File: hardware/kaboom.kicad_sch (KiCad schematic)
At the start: 40 parts, among them SW1 SW_DP3T

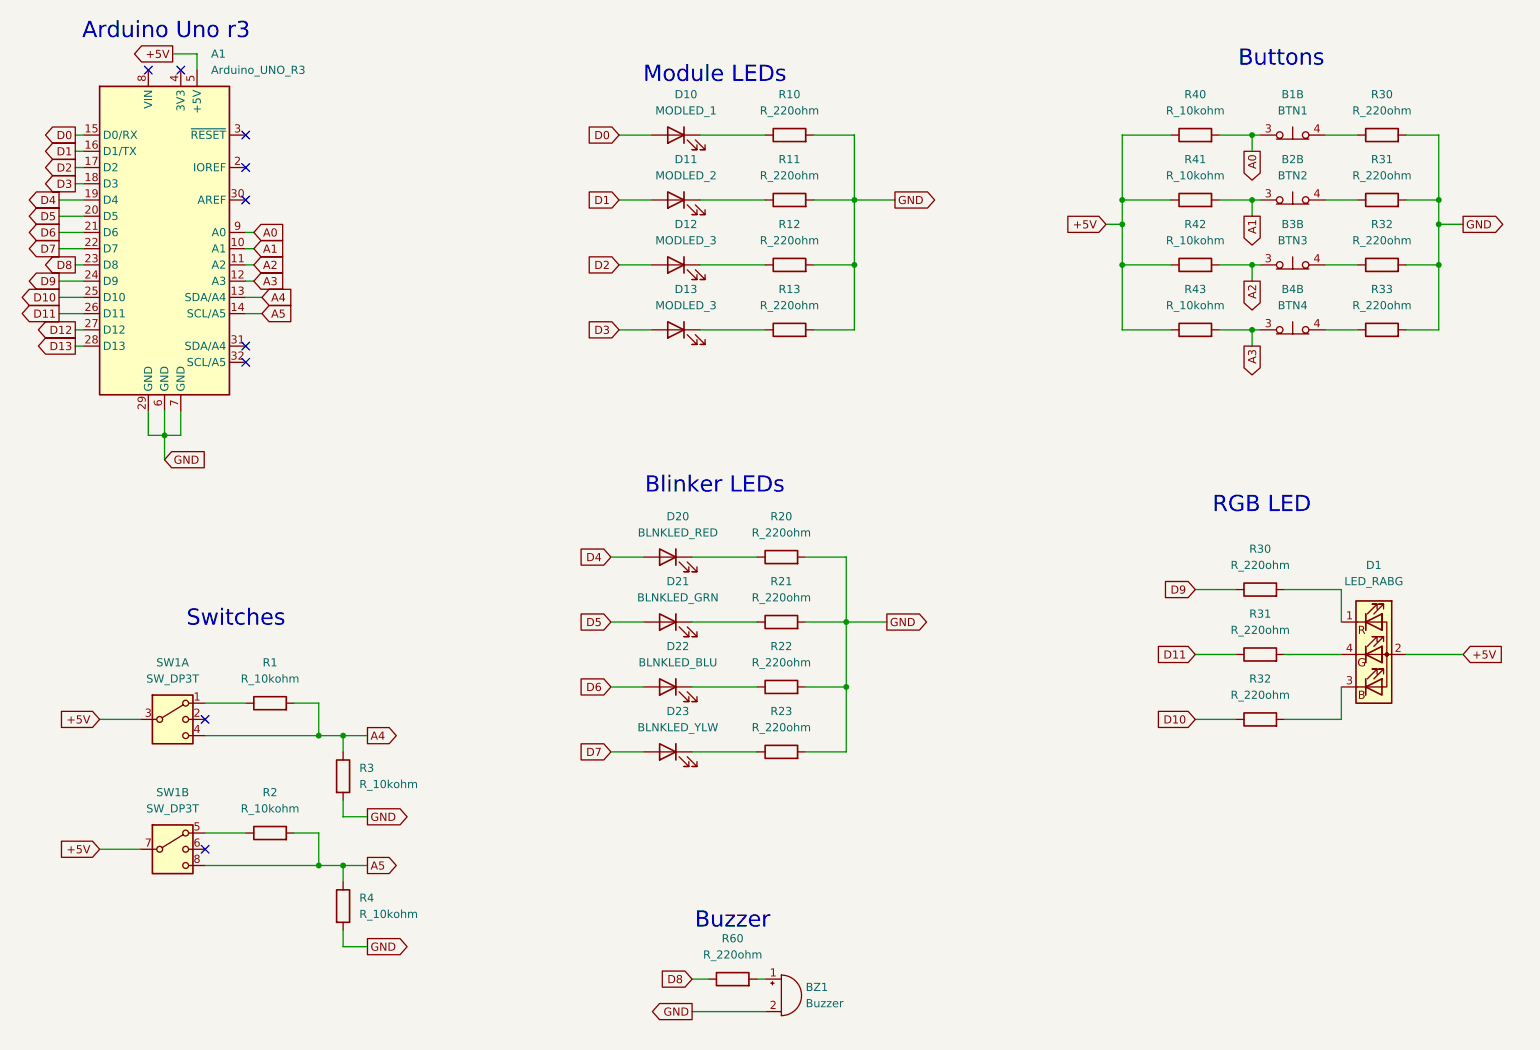
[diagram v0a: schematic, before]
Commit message: Updated coupling diagram
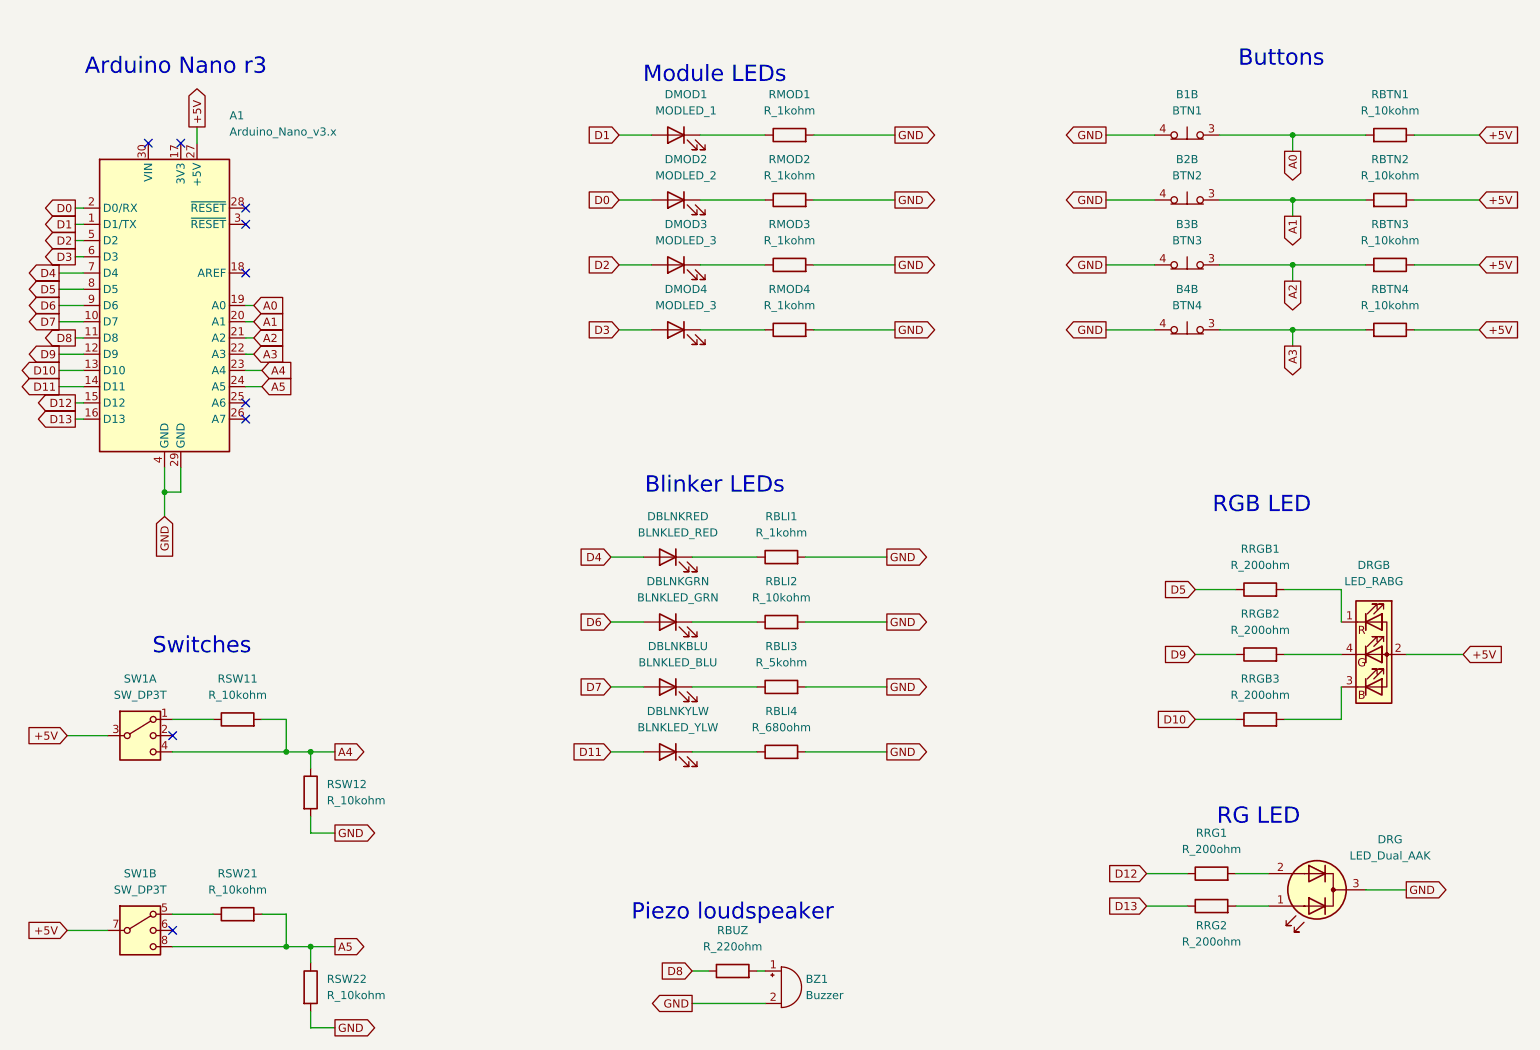
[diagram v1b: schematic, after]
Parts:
- removed A1: Arduino_UNO_R3, Module:Arduino_UNO_R3, symbol MCU_Module:Arduino_UNO_R3
- removed R30, R31, R32, R33: R_220ohm, symbol Device:R
- added A1: Arduino_Nano_v3.x, Module:Arduino_Nano, symbol MCU_Module:Arduino_Nano_v3.x
- added DRG: LED_Dual_AAK, symbol Device:LED_Dual_AAK
- added RRG1, RRG2: R_200ohm, symbol Device:R
- RBLI1: renamed from R20; value R_220ohm -> R_1kohm
- RBLI2: renamed from R21; value R_220ohm -> R_10kohm
- RBLI3: renamed from R22; value R_220ohm -> R_5kohm
- RBLI4: renamed from R23; value R_220ohm -> R_680ohm
- RMOD1: renamed from R10; value R_220ohm -> R_1kohm
- RMOD2: renamed from R11; value R_220ohm -> R_1kohm
- RMOD3: renamed from R12; value R_220ohm -> R_1kohm
- RMOD4: renamed from R13; value R_220ohm -> R_1kohm
- RRGB1: renamed from R30; value R_220ohm -> R_200ohm
- RRGB2: renamed from R31; value R_220ohm -> R_200ohm
- RRGB3: renamed from R32; value R_220ohm -> R_200ohm
- renumbered D22 to DBLNKBLU, D21 to DBLNKGRN, D20 to DBLNKRED, D23 to DBLNKYLW, D10 to DMOD1, D11 to DMOD2, D12 to DMOD3, D13 to DMOD4, D1 to DRGB, R40 to RBTN1, R41 to RBTN2, R42 to RBTN3, R43 to RBTN4, R60 to RBUZ, R1 to RSW11, R3 to RSW12, R2 to RSW21, R4 to RSW22
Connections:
- net +5V: now also A1.27 (+5V)
- net A0: now also A1.19 (A0)
- net A1: now also A1.20 (A1)
- net A2: now also A1.21 (A2)
- net A3: now also A1.22 (A3)
- net A4: now also A1.23 (A4)
- net A5: now also A1.24 (A5)
- net D0: now also DMOD2.2 (A), A1.2 (D0/RX); no longer DMOD1.2 (A)
- net D1: now also DMOD1.2 (A), A1.1 (D1/TX); no longer DMOD2.2 (A)
- net D10: now also A1.13 (D10)
- net D11: now also DBLNKYLW.2 (A), A1.14 (D11); no longer RRGB2.1
- net D12: now also A1.15 (D12), RRG1.1
- net D13: now also A1.16 (D13), RRG2.1
- net D2: now also A1.5 (D2)
- net D3: now also A1.6 (D3)
- net D4: now also A1.7 (D4)
- net D5: now also RRGB1.1, A1.8 (D5); no longer DBLNKGRN.2 (A)
- net D6: now also DBLNKGRN.2 (A), A1.9 (D6); no longer DBLNKBLU.2 (A)
- net D7: now also DBLNKBLU.2 (A), A1.10 (D7); no longer DBLNKYLW.2 (A)
- net D8: now also A1.11 (D8)
- net D9: now also RRGB2.1, A1.12 (D9); no longer RRGB1.1
- net GND: now also B1.4 (2), B2.4 (2), B3.4 (2), B4.4 (2), A1.29 (GND), A1.4 (GND), DRG.3 (K)
- new net: DRG.1 (A1), RRG2.2
- new net: DRG.2 (A2), RRG1.2
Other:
- note added: "Arduino Nano r3"
- note added: "Piezo loudspeaker"
- note added: "RG LED"
- note removed: "Arduino Uno r3"
- note removed: "Buzzer"
- title: Kaboom coupling diagram -> BoomKah coupling diagram
- moved on the sheet: B1B, B2B, B3B, B4B, BZ1, RBTN1, RBTN2, RBTN3, RBTN4, RBUZ, RSW11, RSW12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
